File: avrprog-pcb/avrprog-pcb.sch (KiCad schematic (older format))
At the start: 28 parts, among them J1 Conn_01x04, J2 em_clk, U1 FT232RL, U2 ATmega8A-PU

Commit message: creating PCB
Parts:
- added C8, C9: 22pF, Capacitor_THT:C_Disc_D5.0mm_W2.5mm_P2.50mm, symbol Device:C_Small
- added D8: prgpwr, LED_THT:LED_D3.0mm, symbol Device:LED_Small
- added J3: selfprog, Connector_PinHeader_2.54mm:PinHeader_2x03_P2.54mm_Vertical, symbol Connector_Generic:Conn_02x03_Odd_Even
- added J4: prog, Connector_PinHeader_2.54mm:PinHeader_2x05_P2.54mm_Vertical, symbol Connector_Generic:Conn_02x05_Odd_Even
- added JP2: prog_jmp, Connector_PinHeader_2.54mm:PinHeader_1x02_P2.54mm_Vertical, symbol Device:Jumper_NO_Small
- added JP3: progpwr, Connector_PinHeader_2.54mm:PinHeader_1x02_P2.54mm_Vertical, symbol Device:Jumper_NO_Small
- added R10, R11, R12, R13, R14, R15, R16, R17, R9: 1K, Resistor_THT:R_Axial_DIN0207_L6.3mm_D2.5mm_P10.16mm_Horizontal, symbol Device:R_Small
- added Y1: 7.3728MHz, Crystal:Crystal_HC49-U_Vertical, symbol Device:Crystal_Small
- C1, C2, C3, C4, C5, C7: footprint (none) -> Capacitor_THT:C_Disc_D5.0mm_W2.5mm_P2.50mm
- C6: footprint (none) -> Capacitor_THT:CP_Radial_D6.3mm_P2.50mm
- D1, D2, D3, D4, D5, D6: footprint (none) -> LED_THT:LED_D3.0mm
- D7: footprint (none) -> Diode_THT:D_DO-35_SOD27_P7.62mm_Horizontal
- J1: value Conn_01x04 -> usb
- L1: value L_Core_Ferrite_Small -> 10mH; footprint (none) -> Inductor_THT:L_Axial_L6.6mm_D2.7mm_P10.16mm_Horizontal_Vishay_IM-2
- R1, R2, R3, R4, R5, R6, R7, R8: footprint (none) -> Resistor_THT:R_Axial_DIN0207_L6.3mm_D2.5mm_P10.16mm_Horizontal
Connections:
- net AT_RESET: now also J3.5 (Pin_5), JP2.2
- net AT_RXD: now also R11.2
- net AT_TXD: now also R12.2
- net GND: now also C8.2, C9.2, D8.1 (K), J3.6 (Pin_6), J4.10 (Pin_10), J4.4 (Pin_4), J4.6 (Pin_6), J4.8 (Pin_8)
- net VCC: now also J3.2 (Pin_2), JP3.1
- net USBDM: now reaches J1.3 (Pin_3)
- net USBDM: now also U1.16 (USBD-); no longer U1.15 (USBD+)
- net USBDP: now reaches J1.4 (Pin_4)
- net USBDP: now also U1.15 (USBD+); no longer U1.16 (USBD-)
- net FT_DTR: now reaches U1.2 (DTR)
- net FT_DTR: now also R10.2
- net FT_RTS: now reaches U1.3 (RTS)
- net FT_RTS: now also R9.2
- net at U2.10 (PB7/XTAL2): now also C9.1, Y1.2
- net AT_MOSI: now reaches U2.17 (PB3)
- net AT_MOSI: now also J3.4 (Pin_4), R9.1
- net AT_MISO: now reaches U2.18 (PB4)
- net AT_MISO: now also J3.1 (Pin_1), R12.1
- net AT_SCK: now reaches U2.19 (PB5)
- net AT_SCK: now also J3.3 (Pin_3), R11.1
- net PRG_MISO: now reaches U2.25 (PC2)
- net PRG_MISO: now also R17.2
- net PRG_SCK: now reaches U2.26 (PC3)
- net PRG_SCK: now also R16.2
- net PRG_RESET: now reaches U2.27 (PC4)
- net PRG_RESET: now also R15.2
- net PRG_MOSI: now reaches U2.28 (PC5)
- net PRG_MOSI: now also R14.2
- net at U2.9 (PB6/XTAL1): now also C8.1, Y1.1
- new net: JP2.1, R10.1
- new net: J4.1 (Pin_1), R14.1
- new net: J4.2 (Pin_2), JP3.2, R13.1
- new net: J4.5 (Pin_5), R15.1
- new net: J4.7 (Pin_7), R16.1
- new net: J4.9 (Pin_9), R17.1
- new net: D8.2 (A), R13.2
- no-connect marks 16 -> 17
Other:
- moved on the sheet: C3, C4, C7, D4, D5, D6, D7, J2, JP1, R5, R6, R7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

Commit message: designing PCB
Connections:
- net PRG_MISO: now also U2.28 (PC5); no longer U2.25 (PC2)
- net PRG_MOSI: now also U2.25 (PC2); no longer U2.28 (PC5)
- net PRG_RESET: now also U2.26 (PC3); no longer U2.27 (PC4)
- net PRG_SCK: now also U2.27 (PC4); no longer U2.26 (PC3)
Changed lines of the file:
@@
 Text GLabel 9400 3450 0    50   Input ~ 0
 PRG_MOSI
-Text GLabel 8200 3950 2    50   Input ~ 0
+Text GLabel 8200 3650 2    50   Input ~ 0
 PRG_MOSI
-Text GLabel 8200 3850 2    50   Input ~ 0
+Text GLabel 8200 3750 2    50   Input ~ 0
 PRG_RESET
 Text GLabel 9400 3650 0    50   Input ~ 0
 PRG_RESET
-Text GLabel 8200 3750 2    50   Input ~ 0
+Text GLabel 8200 3850 2    50   Input ~ 0
 PRG_SCK
 Text GLabel 9400 3750 0    50   Input ~ 0
 PRG_SCK
-Text GLabel 8200 3650 2    50   Input ~ 0
+Text GLabel 8200 3950 2    50   Input ~ 0
 PRG_MISO
 Text GLabel 9400 3850 0    50   Input ~ 0

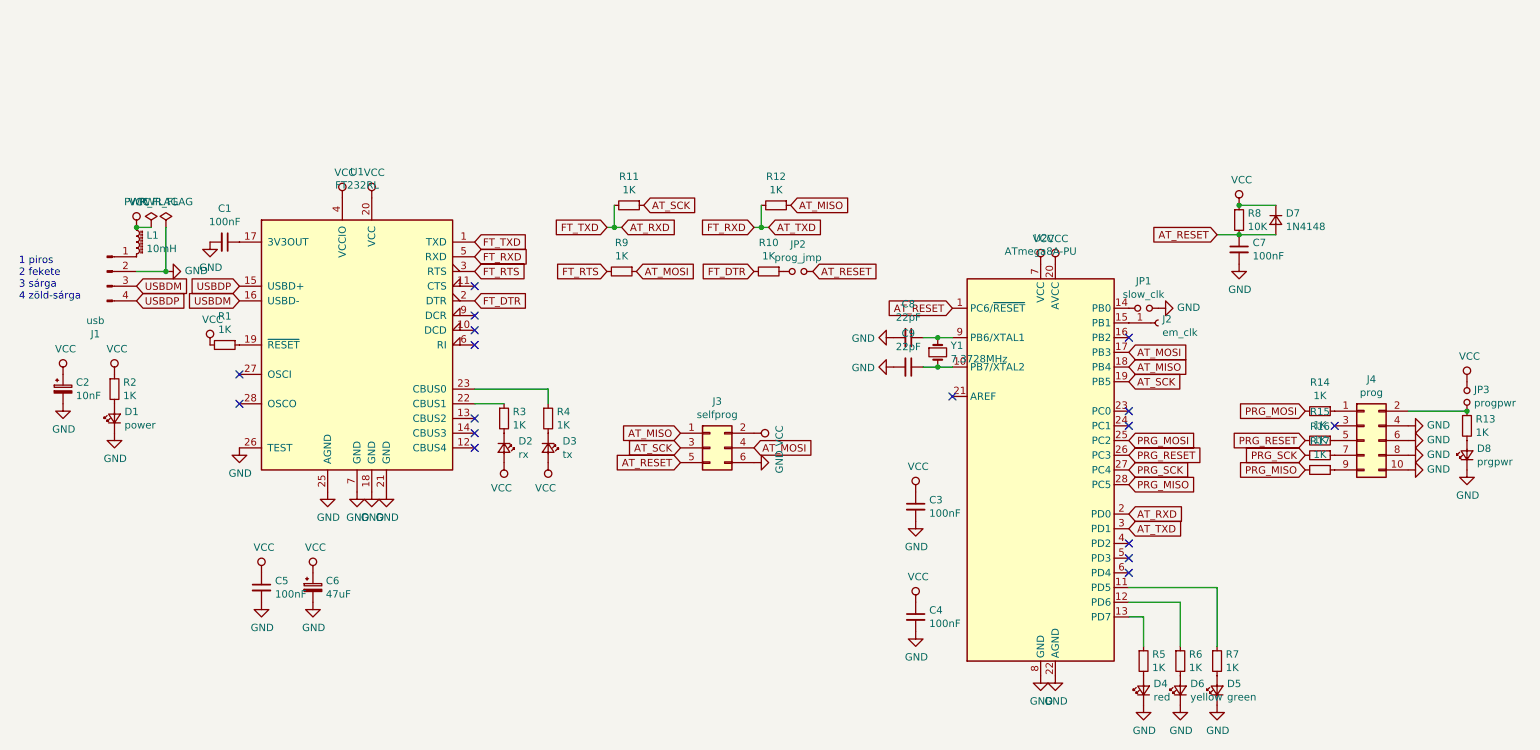
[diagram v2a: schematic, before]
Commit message: minor schematics fixes
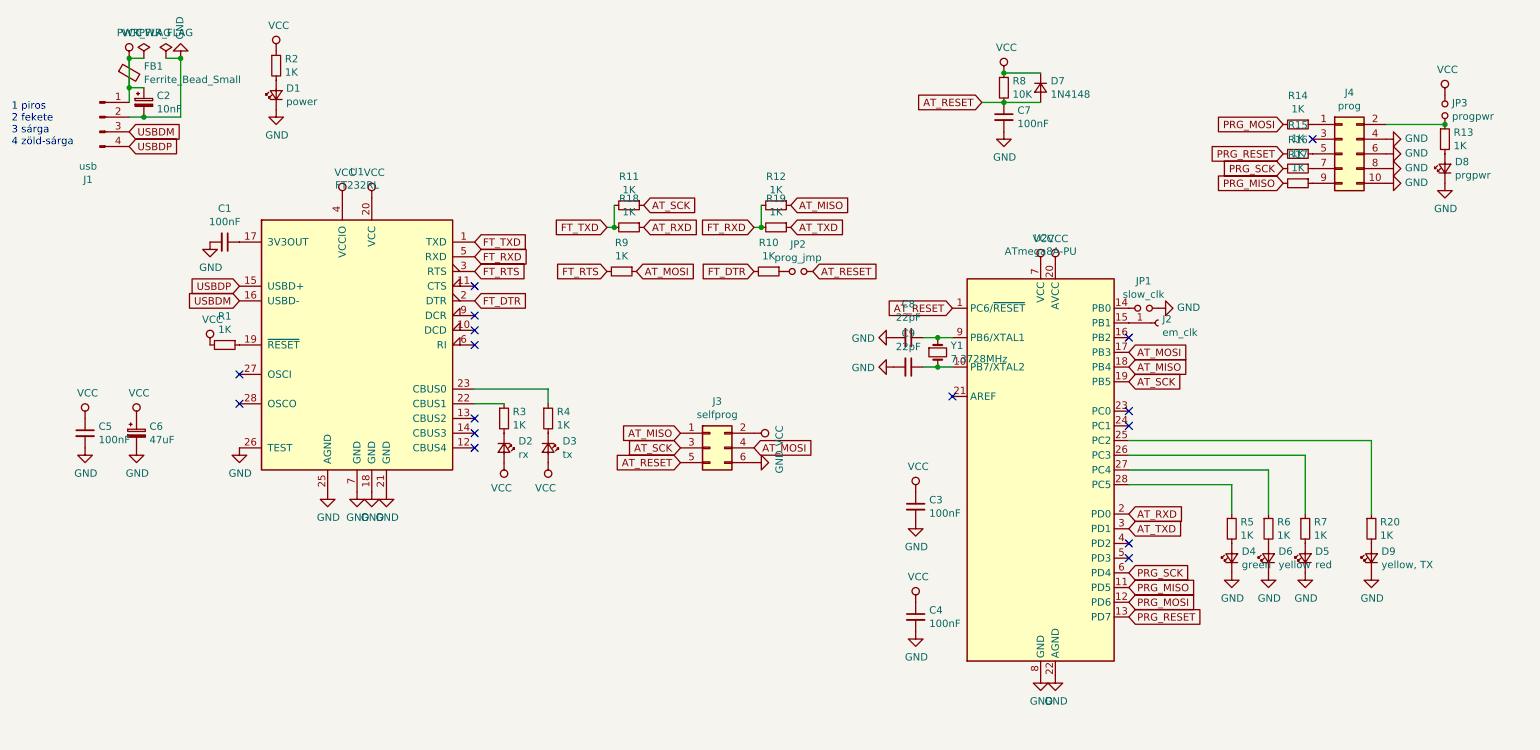
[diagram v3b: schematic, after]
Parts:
- removed L1: 10mH, Inductor_THT:L_Axial_L6.6mm_D2.7mm_P10.16mm_Horizontal_Vishay_IM-2, symbol Device:L_Core_Ferrite_Small
- added D9: yellow, TX, LED_THT:LED_D3.0mm, symbol Device:LED_Small
- added FB1: Ferrite_Bead_Small, symbol Device:Ferrite_Bead_Small
- added R18, R19, R20: 1K, Resistor_THT:R_Axial_DIN0207_L6.3mm_D2.5mm_P10.16mm_Horizontal, symbol Device:R_Small
- D4: value red -> green
- D5: value green -> red
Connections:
- net AT_RXD: now also R18.1; no longer R11.2, U1.1 (TXD)
- net AT_TXD: now also R19.1; no longer R12.2, U1.5 (RXD)
- net GND: now also D9.1 (K)
- net PRG_MISO: now also U2.11 (PD5); no longer U2.28 (PC5)
- net PRG_MOSI: now also U2.12 (PD6); no longer U2.25 (PC2)
- net PRG_RESET: now also U2.13 (PD7); no longer U2.26 (PC3)
- net PRG_SCK: now also U2.6 (PD4); no longer U2.27 (PC4)
- net VCC: now also J1.1 (Pin_1), FB1.1, FB1.2
- net at R7.1: now also U2.26 (PC3); no longer U2.11 (PD5)
- net at R6.1: now also U2.27 (PC4); no longer U2.12 (PD6)
- net at R5.1: now also U2.28 (PC5); no longer U2.13 (PD7)
- new net: R20.1, U2.25 (PC2)
- new net: D9.2 (A), R20.2
- new net FT_RXD: R12.2, R19.2, U1.5 (RXD)
- new net FT_TXD: R11.2, R18.2, U1.1 (TXD)
- no-connect marks 17 -> 16
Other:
- moved on the sheet: C2, C5, C6, C7, D1, D4, D5, D6, D7, D8, J1, J4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

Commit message: schematics and PCB mod
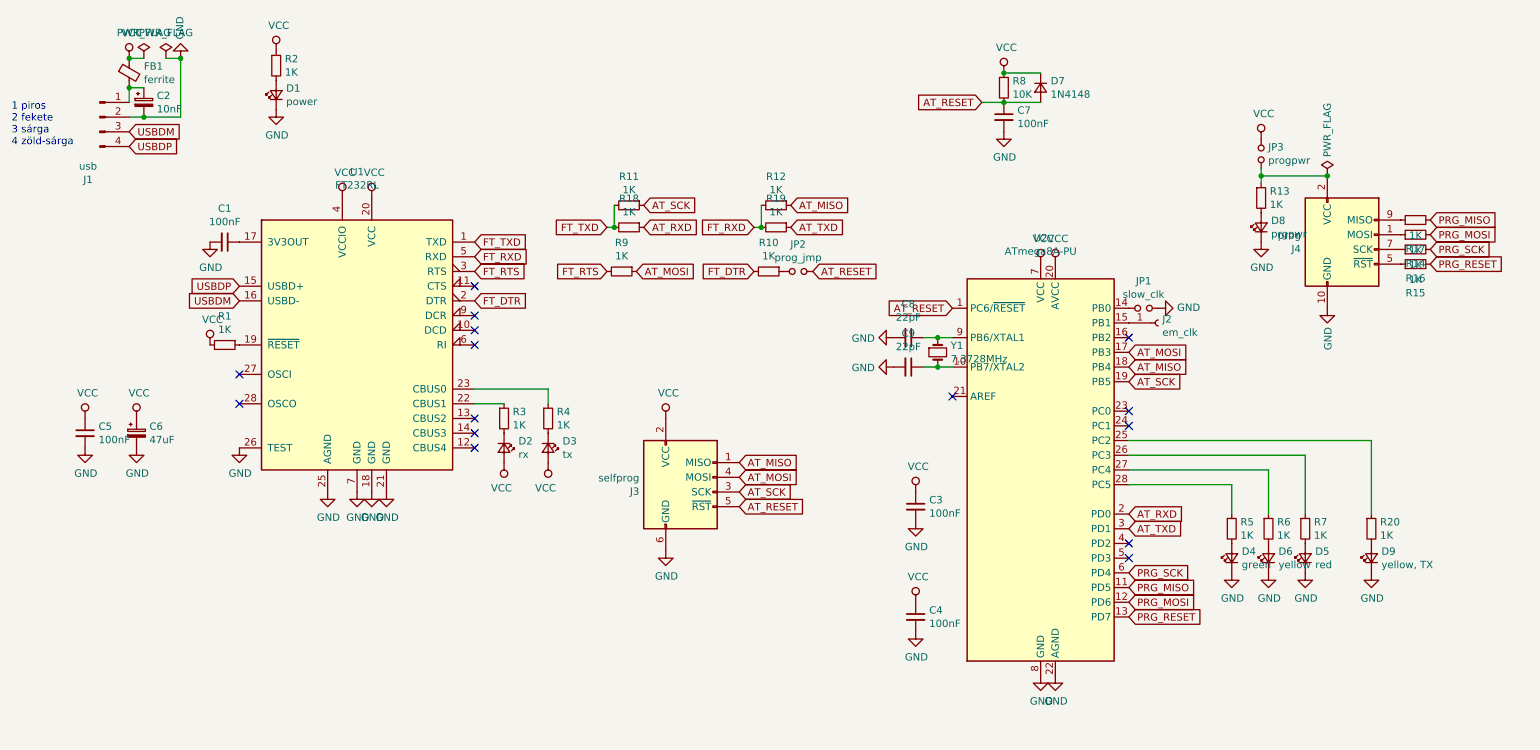
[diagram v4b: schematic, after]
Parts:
- removed J3: selfprog, Connector_PinHeader_2.54mm:PinHeader_2x03_P2.54mm_Vertical, symbol Connector_Generic:Conn_02x03_Odd_Even
- removed J4: prog, Connector_PinHeader_2.54mm:PinHeader_2x05_P2.54mm_Vertical, symbol Connector_Generic:Conn_02x05_Odd_Even
- added J3: selfprog, Connector_PinHeader_2.54mm:PinHeader_2x03_P2.54mm_Vertical, symbol Connector:AVR-ISP-6
- added J4: prog, Connector_PinHeader_2.54mm:PinHeader_2x05_P2.54mm_Vertical, symbol Connector:AVR-ISP-10
- FB1: value Ferrite_Bead_Small -> ferrite; footprint (none) -> Inductor_SMD:L_0805_2012Metric_Pad1.15x1.40mm_HandSolder
- J1: footprint Connector_PinHeader_2.54mm:PinHeader_1x04_P2.54mm_Vertical -> Connector_PinHeader_2.54mm:PinHeader_1x04_P2.54mm_Horizontal
- R1, R10, R11, R12, R13, R14, R15, R16, R17, R18, R19, R2, R20, R3, R4, R5, R6, R7, R8, R9: footprint Resistor_THT:R_Axial_DIN0207_L6.3mm_D2.5mm_P10.16mm_Horizontal -> Resistor_THT:R_Axial_DIN0207_L6.3mm_D2.5mm_P7.62mm_Horizontal
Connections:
- net AT_MISO: now also J3.1 (MISO)
- net AT_MOSI: now also J3.4 (MOSI)
- net AT_RESET: now also J3.5 (~RST)
- net AT_SCK: now also J3.3 (SCK)
- net GND: now also J3.6 (GND), J4.10 (GND), J4.4 (GND), J4.6 (GND), J4.8 (GND)
- net VCC: now also J3.2 (VCC); no longer C2.1, FB1.2, J1.1 (Pin_1)
- net at R14.1: now also J4.1 (MOSI)
- net at JP3.2, R13.1: now also J4.2 (VCC)
- net at R15.1: now also J4.5 (~RST)
- net at R16.1: now also J4.7 (SCK)
- net at R17.1: now also J4.9 (MISO)
- new net: C2.1, FB1.2, J1.1 (Pin_1)
- no-connect marks 16 -> 15
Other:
- moved on the sheet: D8, JP3, R13, R14, R15, R16, R17

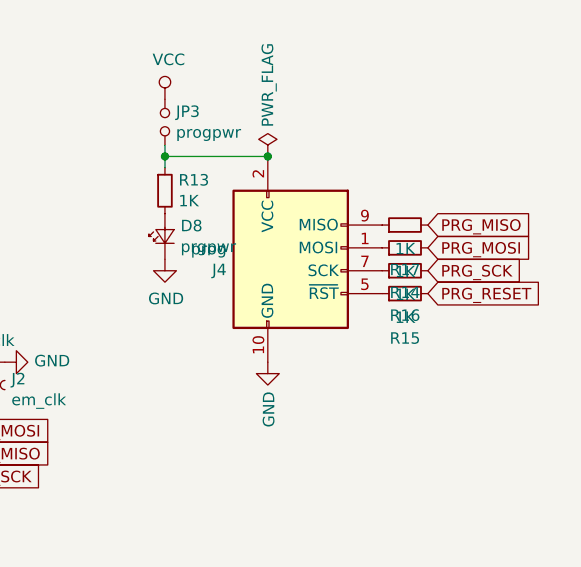
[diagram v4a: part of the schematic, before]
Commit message: schematics and PCB mod connector ISP connector 10 to 6
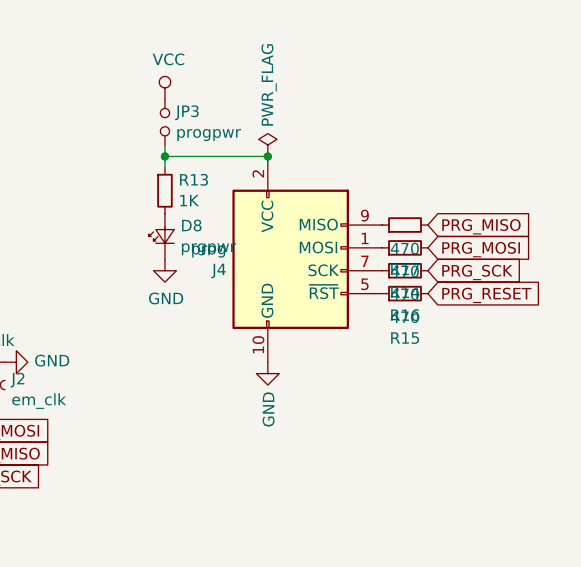
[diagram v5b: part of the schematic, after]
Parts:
- C1, C3, C4, C5, C7: footprint Capacitor_THT:C_Disc_D5.0mm_W2.5mm_P2.50mm -> Capacitor_THT:C_Rect_L7.2mm_W2.5mm_P5.00mm_FKS2_FKP2_MKS2_MKP2
- R14, R15, R16, R17: value 1K -> 470
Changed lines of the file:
@@
 F 0 "C1" V 1821 2300 50  0000 C CNN
 F 1 "100nF" V 1912 2300 50  0000 C CNN
-F 2 "Capacitor_THT:C_Disc_D5.0mm_W2.5mm_P2.50mm" H 2050 2300 50  0001 C CNN
+F 2 "Capacitor_THT:C_Rect_L7.2mm_W2.5mm_P5.00mm_FKS2_FKP2_MKS2_MKP2" H 2050 2300 50  0001 C CNN
 F 3 "~" H 2050 2300 50  0001 C CNN
 	1    2050 2300
@@
 F 0 "C4" H 6842 4896 50  0000 L CNN
 F 1 "100nF" H 6842 4805 50  0000 L CNN
-F 2 "Capacitor_THT:C_Disc_D5.0mm_W2.5mm_P2.50mm" H 6788 4700 50  0001 C CNN
+F 2 "Capacitor_THT:C_Rect_L7.2mm_W2.5mm_P5.00mm_FKS2_FKP2_MKS2_MKP2" H 6788 4700 50  0001 C CNN
 F 3 "~" H 6750 4850 50  0001 C CNN
 	1    6750 4850
@@
 F 0 "C3" H 6842 4146 50  0000 L CNN
 F 1 "100nF" H 6842 4055 50  0000 L CNN
-F 2 "Capacitor_THT:C_Disc_D5.0mm_W2.5mm_P2.50mm" H 6788 3950 50  0001 C CNN
+F 2 "Capacitor_THT:C_Rect_L7.2mm_W2.5mm_P5.00mm_FKS2_FKP2_MKS2_MKP2" H 6788 3950 50  0001 C CNN
 F 3 "~" H 6750 4100 50  0001 C CNN
 	1    6750 4100
@@
 F 0 "C5" H 1192 3646 50  0000 L CNN
 F 1 "100nF" H 1192 3555 50  0000 L CNN
-F 2 "Capacitor_THT:C_Disc_D5.0mm_W2.5mm_P2.50mm" H 1100 3600 50  0001 C CNN
+F 2 "Capacitor_THT:C_Rect_L7.2mm_W2.5mm_P5.00mm_FKS2_FKP2_MKS2_MKP2" H 1100 3600 50  0001 C CNN
 F 3 "~" H 1100 3600 50  0001 C CNN
 	1    1100 3600
@@
 F 0 "C7" H 7442 1496 50  0000 L CNN
 F 1 "100nF" H 7442 1405 50  0000 L CNN
-F 2 "Capacitor_THT:C_Disc_D5.0mm_W2.5mm_P2.50mm" H 7350 1450 50  0001 C CNN
+F 2 "Capacitor_THT:C_Rect_L7.2mm_W2.5mm_P5.00mm_FKS2_FKP2_MKS2_MKP2" H 7350 1450 50  0001 C CNN
 F 3 "~" H 7350 1450 50  0001 C CNN
 	1    7350 1450
@@
 P 10150 2350
 F 0 "R16" V 9954 2350 50  0000 C CNN
-F 1 "1K" V 10045 2350 50  0000 C CNN
+F 1 "470" V 10045 2350 50  0000 C CNN
 F 2 "Resistor_THT:R_Axial_DIN0207_L6.3mm_D2.5mm_P7.62mm_Horizontal" H 10150 2350 50  0001 C CNN
 F 3 "~" H 10150 2350 50  0001 C CNN
@@
 P 10150 2450
 F 0 "R15" V 9954 2450 50  0000 C CNN
-F 1 "1K" V 10045 2450 50  0000 C CNN
+F 1 "470" V 10045 2450 50  0000 C CNN
 F 2 "Resistor_THT:R_Axial_DIN0207_L6.3mm_D2.5mm_P7.62mm_Horizontal" H 10150 2450 50  0001 C CNN
 F 3 "~" H 10150 2450 50  0001 C CNN
@@
 P 10150 2150
 F 0 "R17" V 9954 2150 50  0000 C CNN
-F 1 "1K" V 10045 2150 50  0000 C CNN
+F 1 "470" V 10045 2150 50  0000 C CNN
 F 2 "Resistor_THT:R_Axial_DIN0207_L6.3mm_D2.5mm_P7.62mm_Horizontal" H 10150 2150 50  0001 C CNN
 F 3 "~" H 10150 2150 50  0001 C CNN
@@
 P 10150 2250
 F 0 "R14" V 9954 2250 50  0000 C CNN
-F 1 "1K" V 10045 2250 50  0000 C CNN
+F 1 "470" V 10045 2250 50  0000 C CNN
 F 2 "Resistor_THT:R_Axial_DIN0207_L6.3mm_D2.5mm_P7.62mm_Horizontal" H 10150 2250 50  0001 C CNN
 F 3 "~" H 10150 2250 50  0001 C CNN
